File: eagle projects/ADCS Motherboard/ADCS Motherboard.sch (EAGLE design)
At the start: 141 parts, among them J1 HDR_10_EZFET_DEBUGGER, J11 CNC_3221-10-0300-00, J5 CNC_3221-10-0300-00, J7 TE-1734829-3, Q1 BSR802NL6327HTSA1, U1 MSP430F5529IPN, U10 TSV991AILT, U2 TSV991AILT, U3 ADS7841E_2K5, U4 TSV991AILT, U5 DMC4050SSDQ-13, U7 HMC1053, U9 BMX160, Y1 32.768kHz, Y2 CSTCR4M00G15L99, Y3 32.768kHz

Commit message: I thinks its done
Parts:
- added R34, R35, R39: 5.1M, rcl:R-US_R0402
- R37: device rcl:R-US_R0805 -> rcl:R-US_R0603
- R55: device rcl:R-US_R0603 -> rcl:R-US_R0402
- U6: value (none) -> BNO055
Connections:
- removed net N$2: C32.1, U9.VDDIO
- removed net N$41: U1.P3.7/TB0OUTH/SVMOUT
- removed net TB0.3: U1.P7.5/TB0.3
- removed net TB0.4: U1.P7.6/TB0.4
- net !CS!_SUN_Z-: now also U1.P6.6/CB6/A6; no longer U1.PJ.3/TCK
- net +3V3: now also C32.1, U9.VDDIO
- net BMX160_INT2: now also R34.2
- net GND: now also R34.1, R35.1, R39.1
- net N$16: now also R35.2
- net N$17: now also R39.2
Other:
- note added: "B"
- note added: "Thomas Christison"
- note removed: "A.1"
- note removed: "BMX160_INT2"

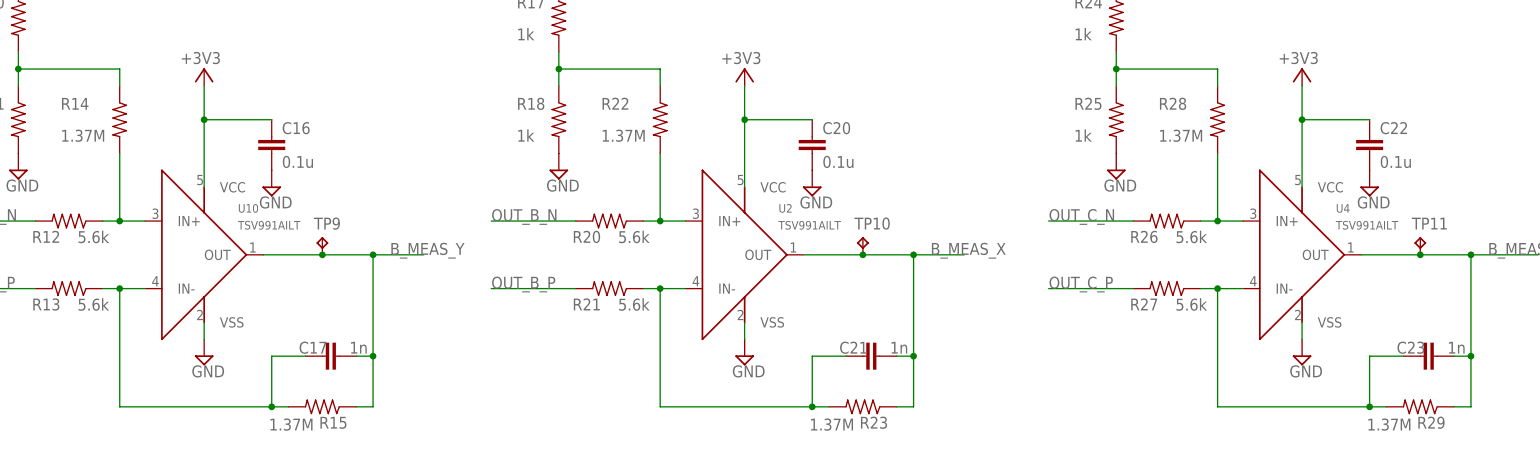
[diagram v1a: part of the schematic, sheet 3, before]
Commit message: silk screen
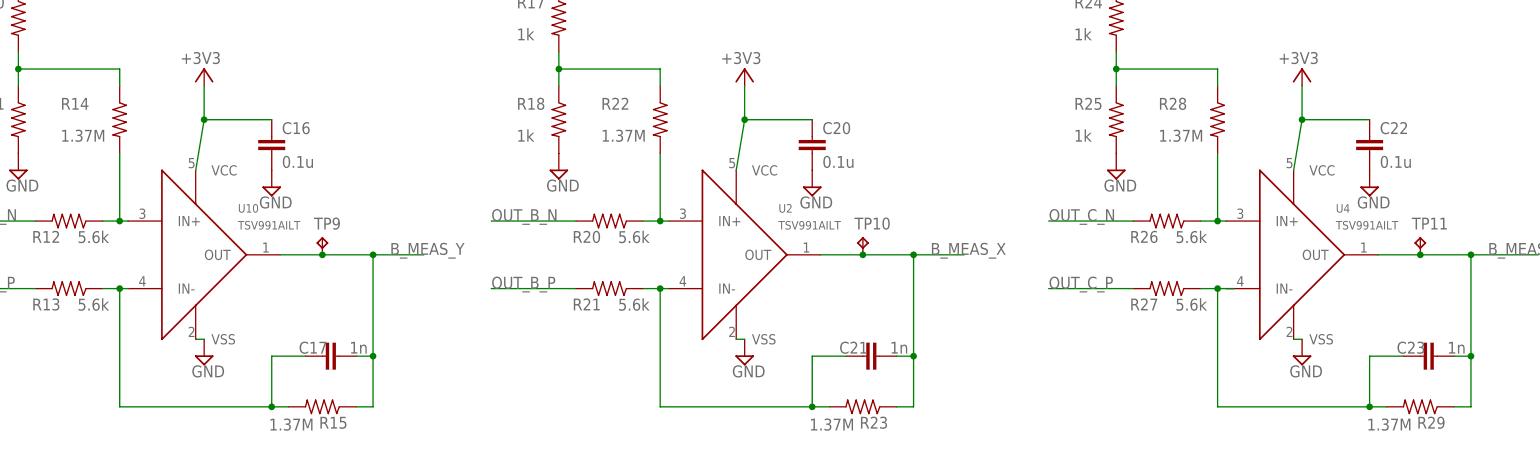
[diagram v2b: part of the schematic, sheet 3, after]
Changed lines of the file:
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@@
 <part name="SUPPLY55" library="supply2" library_urn="urn:adsk.eagle:library:372" deviceset="GND" device=""/>
 <part name="U7" library="my_library" library_urn="urn:adsk.eagle:library:22876504" deviceset="HMC1053" device="" package3d_urn="urn:adsk.eagle:package:22876506/2" value="HMC1053"/>
-<part name="U3" library="my_library" library_urn="urn:adsk.eagle:library:22876504" deviceset="ADS7841E_2K5" device="" package3d_urn="urn:adsk.eagle:package:23087509/6"/>
+<part name="U3" library="my_library" library_urn="urn:adsk.eagle:library:22876504" deviceset="ADS7841E_2K5" device="" package3d_urn="urn:adsk.eagle:package:23087509/8"/>
 <part name="C11" library="rcl" library_urn="urn:adsk.eagle:library:334" deviceset="C-EU" device="C0603" package3d_urn="urn:adsk.eagle:package:23616/2" value="0.1u"/>
 <part name="C14" library="rcl" library_urn="urn:adsk.eagle:library:334" deviceset="C-EU" device="C0603" package3d_urn="urn:adsk.eagle:package:23616/2" value="0.1u"/>
@@
 <part name="U4" library="my_library" library_urn="urn:adsk.eagle:library:22876504" deviceset="TSV991AILT" device="" package3d_urn="urn:adsk.eagle:package:24426275/2"/>
 <part name="JP1" library="pinhead" library_urn="urn:adsk.eagle:library:325" deviceset="PINHD-2X5" device="" package3d_urn="urn:adsk.eagle:package:22470/2"/>
-<part name="U5" library="my_library" library_urn="urn:adsk.eagle:library:22876504" deviceset="DMC4050SSDQ-13" device=""/>
+<part name="U5" library="my_library" library_urn="urn:adsk.eagle:library:22876504" deviceset="DMC4050SSDQ-13" device="" package3d_urn="urn:adsk.eagle:package:30024713/1"/>
 <part name="SUPPLY57" library="supply2" library_urn="urn:adsk.eagle:library:372" deviceset="GND" device=""/>
 <part name="+3V7" library="supply1" library_urn="urn:adsk.eagle:library:371" deviceset="+3V3" device=""/>
@@
 <wire x1="55.88" y1="121.92" x2="55.88" y2="116.84" width="0.1524" layer="91"/>
 <pinref part="C16" gate="G$1" pin="1"/>
-<wire x1="55.88" y1="116.84" x2="55.88" y2="106.68" width="0.1524" layer="91"/>
+<wire x1="55.88" y1="116.84" x2="54.61" y2="109.22" width="0.1524" layer="91"/>
 <wire x1="55.88" y1="116.84" x2="66.04" y2="116.84" width="0.1524" layer="91"/>
 <junction x="55.88" y="116.84"/>
@@
 <wire x1="137.16" y1="121.92" x2="137.16" y2="116.84" width="0.1524" layer="91"/>
 <pinref part="C20" gate="G$1" pin="1"/>
-<wire x1="137.16" y1="116.84" x2="137.16" y2="106.68" width="0.1524" layer="91"/>
+<wire x1="137.16" y1="116.84" x2="135.89" y2="109.22" width="0.1524" layer="91"/>
 <wire x1="137.16" y1="116.84" x2="147.32" y2="116.84" width="0.1524" layer="91"/>
 <junction x="137.16" y="116.84"/>
@@
 <wire x1="220.98" y1="121.92" x2="220.98" y2="116.84" width="0.1524" layer="91"/>
 <pinref part="C22" gate="G$1" pin="1"/>
-<wire x1="220.98" y1="116.84" x2="220.98" y2="106.68" width="0.1524" layer="91"/>
+<wire x1="220.98" y1="116.84" x2="219.71" y2="109.22" width="0.1524" layer="91"/>
 <wire x1="220.98" y1="116.84" x2="231.14" y2="116.84" width="0.1524" layer="91"/>
 <junction x="220.98" y="116.84"/>
@@
 <pinref part="SUPPLY22" gate="GND" pin="GND"/>
 <pinref part="U10" gate="G$1" pin="VSS"/>
-<wire x1="55.88" y1="83.82" x2="55.88" y2="86.36" width="0.1524" layer="91"/>
+<wire x1="55.88" y1="83.82" x2="54.61" y2="83.82" width="0.1524" layer="91"/>
 </segment>
 <segment>
 <pinref part="SUPPLY28" gate="GND" pin="GND"/>
 <pinref part="U2" gate="G$1" pin="VSS"/>
-<wire x1="137.16" y1="83.82" x2="137.16" y2="86.36" width="0.1524" layer="91"/>
+<wire x1="137.16" y1="83.82" x2="135.89" y2="83.82" width="0.1524" layer="91"/>
 </segment>
 <segment>
 <pinref part="U4" gate="G$1" pin="VSS"/>
 <pinref part="SUPPLY34" gate="GND" pin="GND"/>
-<wire x1="220.98" y1="86.36" x2="220.98" y2="83.82" width="0.1524" layer="91"/>
+<wire x1="219.71" y1="83.82" x2="220.98" y2="83.82" width="0.1524" layer="91"/>
 </segment>
 <segment>
@@
 <wire x1="246.38" y1="96.52" x2="238.76" y2="96.52" width="0.1524" layer="91"/>
 <pinref part="R29" gate="G$1" pin="1"/>
-<wire x1="238.76" y1="96.52" x2="229.87" y2="96.52" width="0.1524" layer="91"/>
+<wire x1="238.76" y1="96.52" x2="232.41" y2="96.52" width="0.1524" layer="91"/>
 <wire x1="243.84" y1="73.66" x2="246.38" y2="73.66" width="0.1524" layer="91"/>
 <wire x1="246.38" y1="96.52" x2="256.54" y2="96.52" width="0.1524" layer="91"/>
@@
 <wire x1="81.28" y1="96.52" x2="73.66" y2="96.52" width="0.1524" layer="91"/>
 <pinref part="R15" gate="G$1" pin="1"/>
-<wire x1="73.66" y1="96.52" x2="64.77" y2="96.52" width="0.1524" layer="91"/>
+<wire x1="73.66" y1="96.52" x2="67.31" y2="96.52" width="0.1524" layer="91"/>
 <wire x1="78.74" y1="73.66" x2="81.28" y2="73.66" width="0.1524" layer="91"/>
 <label x="83.82" y="96.52" size="1.778" layer="95"/>
@@
 <wire x1="162.56" y1="96.52" x2="154.94" y2="96.52" width="0.1524" layer="91"/>
 <pinref part="R23" gate="G$1" pin="1"/>
-<wire x1="154.94" y1="96.52" x2="146.05" y2="96.52" width="0.1524" layer="91"/>
+<wire x1="154.94" y1="96.52" x2="148.59" y2="96.52" width="0.1524" layer="91"/>
 <wire x1="160.02" y1="73.66" x2="162.56" y2="73.66" width="0.1524" layer="91"/>
 <label x="165.1" y="96.52" size="1.778" layer="95"/>
@@
 <pinref part="R13" gate="G$1" pin="1"/>
 <wire x1="40.64" y1="91.44" x2="43.18" y2="91.44" width="0.1524" layer="91"/>
-<wire x1="43.18" y1="91.44" x2="46.99" y2="91.44" width="0.1524" layer="91"/>
+<wire x1="43.18" y1="91.44" x2="44.45" y2="91.44" width="0.1524" layer="91"/>
 <wire x1="43.18" y1="73.66" x2="43.18" y2="91.44" width="0.1524" layer="91"/>
 <junction x="43.18" y="91.44"/>
@@
 <net name="N$23" class="0">
 <segment>
-<wire x1="43.18" y1="101.6" x2="46.99" y2="101.6" width="0.1524" layer="91"/>
+<wire x1="43.18" y1="101.6" x2="44.45" y2="101.6" width="0.1524" layer="91"/>
 <junction x="43.18" y="101.6"/>
 <wire x1="43.18" y1="101.6" x2="43.18" y2="111.76" width="0.1524" layer="91"/>
@@
 <pinref part="R21" gate="G$1" pin="1"/>
 <wire x1="121.92" y1="91.44" x2="124.46" y2="91.44" width="0.1524" layer="91"/>
-<wire x1="124.46" y1="91.44" x2="128.27" y2="91.44" width="0.1524" layer="91"/>
+<wire x1="124.46" y1="91.44" x2="125.73" y2="91.44" width="0.1524" layer="91"/>
 <wire x1="124.46" y1="73.66" x2="124.46" y2="91.44" width="0.1524" layer="91"/>
 <junction x="124.46" y="91.44"/>
@@
 <net name="N$52" class="0">
 <segment>
-<wire x1="124.46" y1="101.6" x2="128.27" y2="101.6" width="0.1524" layer="91"/>
+<wire x1="124.46" y1="101.6" x2="125.73" y2="101.6" width="0.1524" layer="91"/>
 <junction x="124.46" y="101.6"/>
 <wire x1="124.46" y1="101.6" x2="124.46" y2="111.76" width="0.1524" layer="91"/>
@@
 <wire x1="205.74" y1="91.44" x2="208.28" y2="91.44" width="0.1524" layer="91"/>
 <wire x1="208.28" y1="91.44" x2="209.55" y2="91.44" width="0.1524" layer="91"/>
-<wire x1="209.55" y1="91.44" x2="210.82" y2="91.44" width="0.1524" layer="91"/>
 <wire x1="208.28" y1="73.66" x2="208.28" y2="91.44" width="0.1524" layer="91"/>
 <junction x="208.28" y="91.44"/>
@@
 <junction x="231.14" y="73.66"/>
 <pinref part="U4" gate="G$1" pin="IN-"/>
-<wire x1="212.09" y1="91.44" x2="210.82" y2="91.44" width="0.1524" layer="91"/>
+<wire x1="209.55" y1="91.44" x2="210.82" y2="91.44" width="0.1524" layer="91"/>
 </segment>
 </net>
 <net name="N$62" class="0">
 <segment>
-<wire x1="208.28" y1="101.6" x2="212.09" y2="101.6" width="0.1524" layer="91"/>
+<wire x1="208.28" y1="101.6" x2="209.55" y2="101.6" width="0.1524" layer="91"/>
 <junction x="208.28" y="101.6"/>
 <wire x1="208.28" y1="101.6" x2="208.28" y2="111.76" width="0.1524" layer="91"/>

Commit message: finilized rev b layout
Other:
- note added: "ADCS Electrical"
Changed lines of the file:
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@@
 <text x="203.2" y="63.5" size="1.778" layer="97">PWM</text>
 <text x="189.992" y="11.43" size="2.54" layer="94">Thomas Christison</text>
+<text x="196.342" y="6.858" size="2.54" layer="94">ADCS Electrical</text>
 </plain>
 <instances>
@@
 <text x="73.66" y="198.12" size="1.778" layer="97">NC</text>
 <text x="189.992" y="11.684" size="2.54" layer="94">Thomas Christison</text>
+<text x="196.088" y="6.604" size="2.54" layer="94">ADCS Electrical</text>
 </plain>
 <instances>
@@
 <text x="40.64" y="152.4" size="1.778" layer="97">Totem Pole Driver (Complementary mosfet pair)</text>
 <text x="190.5" y="11.43" size="2.54" layer="94">Thomas Christison</text>
+<text x="195.58" y="6.35" size="2.54" layer="94">ADCS Electrical</text>
 </plain>
 <instances>
@@
 Set to GND is I2C mode</text>
 <text x="190.246" y="11.176" size="2.54" layer="94">Thomas Christison</text>
+<text x="195.834" y="6.858" size="2.54" layer="94">Thomas Christison</text>
 </plain>
 <instances>

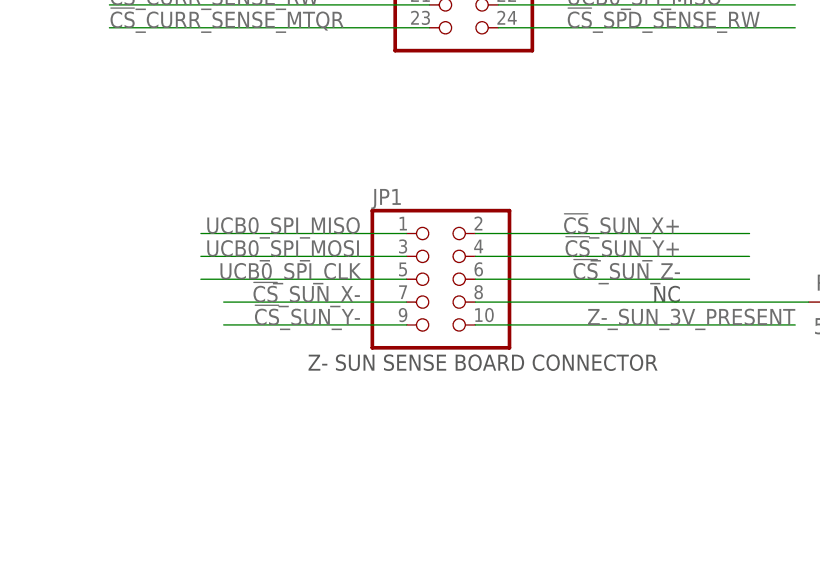
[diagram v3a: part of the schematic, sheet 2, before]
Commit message: Solder Cups on Motherboard
Started swapping connectors on Motherboard
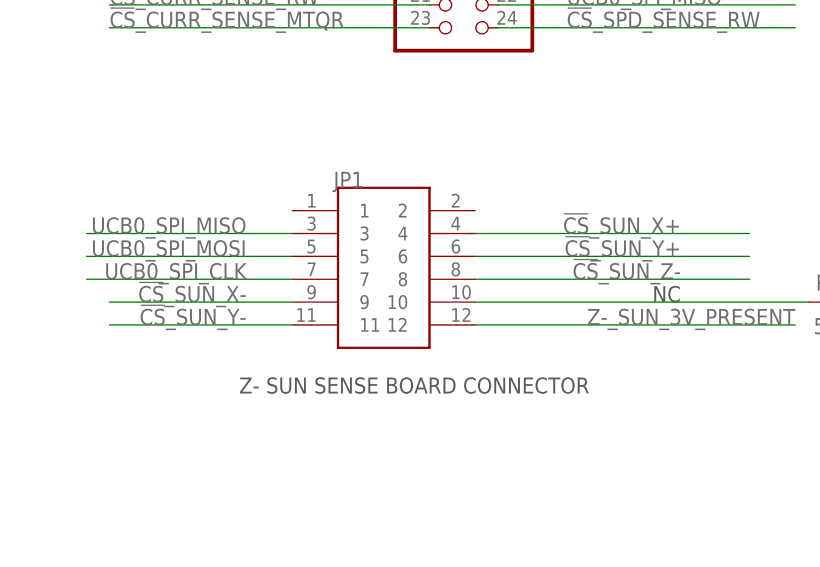
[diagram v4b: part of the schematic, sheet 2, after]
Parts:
- JP1: value (none) -> 832-10-012-10-005000; device pinhead:PINHD-2X5 -> 832-10-012-10-005000:832-10-012-10-005000
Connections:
- net !CS!_SUN_X+: now also JP1.4; no longer JP1.2
- net !CS!_SUN_X-: now also JP1.9; no longer JP1.7
- net !CS!_SUN_Y+: now also JP1.6; no longer JP1.4
- net !CS!_SUN_Y-: now also JP1.11; no longer JP1.9
- net !CS!_SUN_Z-: now also JP1.8; no longer JP1.6
- net N$58: now also JP1.10; no longer JP1.8
- net UCB0_SPI_CLK: now also JP1.7; no longer JP1.5
- net UCB0_SPI_MISO: now also JP1.3; no longer JP1.1
- net UCB0_SPI_MOSI: now also JP1.5; no longer JP1.3
- net Z-_SUN_3V_PRESENT: now also JP1.12; no longer JP1.10
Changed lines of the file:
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@@
 <part name="U2" library="my_library" library_urn="urn:adsk.eagle:library:22876504" deviceset="TSV991AILT" device="" package3d_urn="urn:adsk.eagle:package:24426275/2"/>
 <part name="U4" library="my_library" library_urn="urn:adsk.eagle:library:22876504" deviceset="TSV991AILT" device="" package3d_urn="urn:adsk.eagle:package:24426275/2"/>
-<part name="JP1" library="pinhead" library_urn="urn:adsk.eagle:library:325" deviceset="PINHD-2X5" device="" package3d_urn="urn:adsk.eagle:package:22470/2"/>
 <part name="U5" library="my_library" library_urn="urn:adsk.eagle:library:22876504" deviceset="DMC4050SSDQ-13" device="" package3d_urn="urn:adsk.eagle:package:30024713/1"/>
 <part name="SUPPLY57" library="supply2" library_urn="urn:adsk.eagle:library:372" deviceset="GND" device=""/>
@@
 <part name="SUPPLY60" library="supply2" library_urn="urn:adsk.eagle:library:372" deviceset="GND" device=""/>
 <part name="SUPPLY70" library="supply2" library_urn="urn:adsk.eagle:library:372" deviceset="GND" device=""/>
+<part name="JP1" library="832-10-012-10-005000" deviceset="832-10-012-10-005000" device=""/>
 </parts>
 <sheets>
@@
 <text x="86.36" y="142.24" size="1.778" layer="97" rot="MR0">NC</text>
 <text x="261.62" y="7.62" size="2.54" layer="94">B</text>
-<text x="83.82" y="134.62" size="1.778" layer="97" rot="MR0">Z- SUN SENSE BOARD CONNECTOR</text>
+<text x="76.2" y="132.08" size="1.778" layer="97" rot="MR0">Z- SUN SENSE BOARD CONNECTOR</text>
 <text x="142.24" y="175.26" size="1.778" layer="97">Z+ SUN SENSE BOARD CONNECTOR</text>
 <text x="12.7" y="187.96" size="1.778" layer="97">PWM_OUT</text>
@@
 <attribute name="VALUE" x="54.61" y="167.64" size="1.778" layer="96"/>
 </instance>
-<instance part="JP1" gate="A" x="58.42" y="144.78" smashed="yes">
-<attribute name="NAME" x="52.07" y="153.035" size="1.778" layer="95"/>
-<attribute name="VALUE" x="52.07" y="134.62" size="1.778" layer="96"/>
+<instance part="JP1" gate="G$1" x="53.34" y="147.32" smashed="yes">
+<attribute name="NAME" x="47.76" y="154.94" size="1.778" layer="95"/>
 </instance>
 </instances>
@@
 <net name="UCB0_SPI_CLK" class="0">
 <segment>
-<label x="50.8" y="144.78" size="1.778" layer="95" rot="MR0"/>
-<pinref part="JP1" gate="A" pin="5"/>
-<wire x1="33.02" y1="144.78" x2="55.88" y2="144.78" width="0.1524" layer="91"/>
+<label x="38.1" y="144.78" size="1.778" layer="95" rot="MR0"/>
+<wire x1="20.32" y1="144.78" x2="43.18" y2="144.78" width="0.1524" layer="91"/>
+<pinref part="JP1" gate="G$1" pin="7"/>
 </segment>
 <segment>
@@
 </segment>
 <segment>
-<label x="50.8" y="149.86" size="1.778" layer="95" rot="MR0"/>
-<wire x1="33.02" y1="149.86" x2="55.88" y2="149.86" width="0.1524" layer="91"/>
-<pinref part="JP1" gate="A" pin="1"/>
+<label x="38.1" y="149.86" size="1.778" layer="95" rot="MR0"/>
+<wire x1="20.32" y1="149.86" x2="43.18" y2="149.86" width="0.1524" layer="91"/>
+<pinref part="JP1" gate="G$1" pin="3"/>
 </segment>
 <segment>
@@
 </segment>
 <segment>
-<label x="50.8" y="147.32" size="1.778" layer="95" rot="MR0"/>
-<wire x1="33.02" y1="147.32" x2="55.88" y2="147.32" width="0.1524" layer="91"/>
-<pinref part="JP1" gate="A" pin="3"/>
+<label x="38.1" y="147.32" size="1.778" layer="95" rot="MR0"/>
+<wire x1="20.32" y1="147.32" x2="43.18" y2="147.32" width="0.1524" layer="91"/>
+<pinref part="JP1" gate="G$1" pin="5"/>
 </segment>
 <segment>
@@
 <label x="86.36" y="149.86" size="1.778" layer="95" rot="MR0"/>
 <wire x1="93.98" y1="149.86" x2="63.5" y2="149.86" width="0.1524" layer="91"/>
-<pinref part="JP1" gate="A" pin="2"/>
+<pinref part="JP1" gate="G$1" pin="4"/>
 </segment>
 </net>
 <net name="!CS!_SUN_X-" class="0">
 <segment>
-<label x="50.8" y="142.24" size="1.778" layer="95" rot="MR0"/>
-<pinref part="JP1" gate="A" pin="7"/>
-<wire x1="55.88" y1="142.24" x2="35.56" y2="142.24" width="0.1524" layer="91"/>
+<label x="38.1" y="142.24" size="1.778" layer="95" rot="MR0"/>
+<wire x1="43.18" y1="142.24" x2="22.86" y2="142.24" width="0.1524" layer="91"/>
+<pinref part="JP1" gate="G$1" pin="9"/>
 </segment>
 </net>
 <net name="!CS!_SUN_Y-" class="0">
 <segment>
-<label x="50.8" y="139.7" size="1.778" layer="95" rot="MR0"/>
-<wire x1="35.56" y1="139.7" x2="55.88" y2="139.7" width="0.1524" layer="91"/>
-<pinref part="JP1" gate="A" pin="9"/>
+<label x="38.1" y="139.7" size="1.778" layer="95" rot="MR0"/>
+<wire x1="22.86" y1="139.7" x2="43.18" y2="139.7" width="0.1524" layer="91"/>
+<pinref part="JP1" gate="G$1" pin="11"/>
 </segment>
 </net>
@@
 <segment>
 <label x="86.36" y="144.78" size="1.778" layer="95" rot="MR0"/>
-<pinref part="JP1" gate="A" pin="6"/>
 <wire x1="93.98" y1="144.78" x2="63.5" y2="144.78" width="0.1524" layer="91"/>
+<pinref part="JP1" gate="G$1" pin="8"/>
 </segment>
 </net>
@@
 <segment>
 <label x="86.36" y="147.32" size="1.778" layer="95" rot="MR0"/>
-<pinref part="JP1" gate="A" pin="4"/>
 <wire x1="63.5" y1="147.32" x2="93.98" y2="147.32" width="0.1524" layer="91"/>
+<pinref part="JP1" gate="G$1" pin="6"/>
 </segment>
 </net>
@@
 <label x="99.06" y="139.7" size="1.778" layer="95" rot="MR0"/>
 <wire x1="99.06" y1="139.7" x2="63.5" y2="139.7" width="0.1524" layer="91"/>
-<pinref part="JP1" gate="A" pin="10"/>
+<pinref part="JP1" gate="G$1" pin="12"/>
 </segment>
 </net>
@@
 <segment>
 <pinref part="R45" gate="G$1" pin="1"/>
-<pinref part="JP1" gate="A" pin="8"/>
 <wire x1="63.5" y1="142.24" x2="100.584" y2="142.24" width="0.1524" layer="91"/>
-</segment>
-</net>
+<pinref part="JP1" gate="G$1" pin="10"/>
+</segment>
+</net>
